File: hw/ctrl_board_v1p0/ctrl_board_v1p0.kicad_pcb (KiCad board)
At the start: 2 copper layers, 65 x 30 mm, 31 parts, among them J1 RaSCSI Connector, J2 OLED Connector, P1 Conn_02x20_Odd_Even, SW1 SW_SPST, SW2 SW_SPST, SW3 SW_SPST, SW4 Rotary_Encoder_Switch, U1 PCA9554APW,118

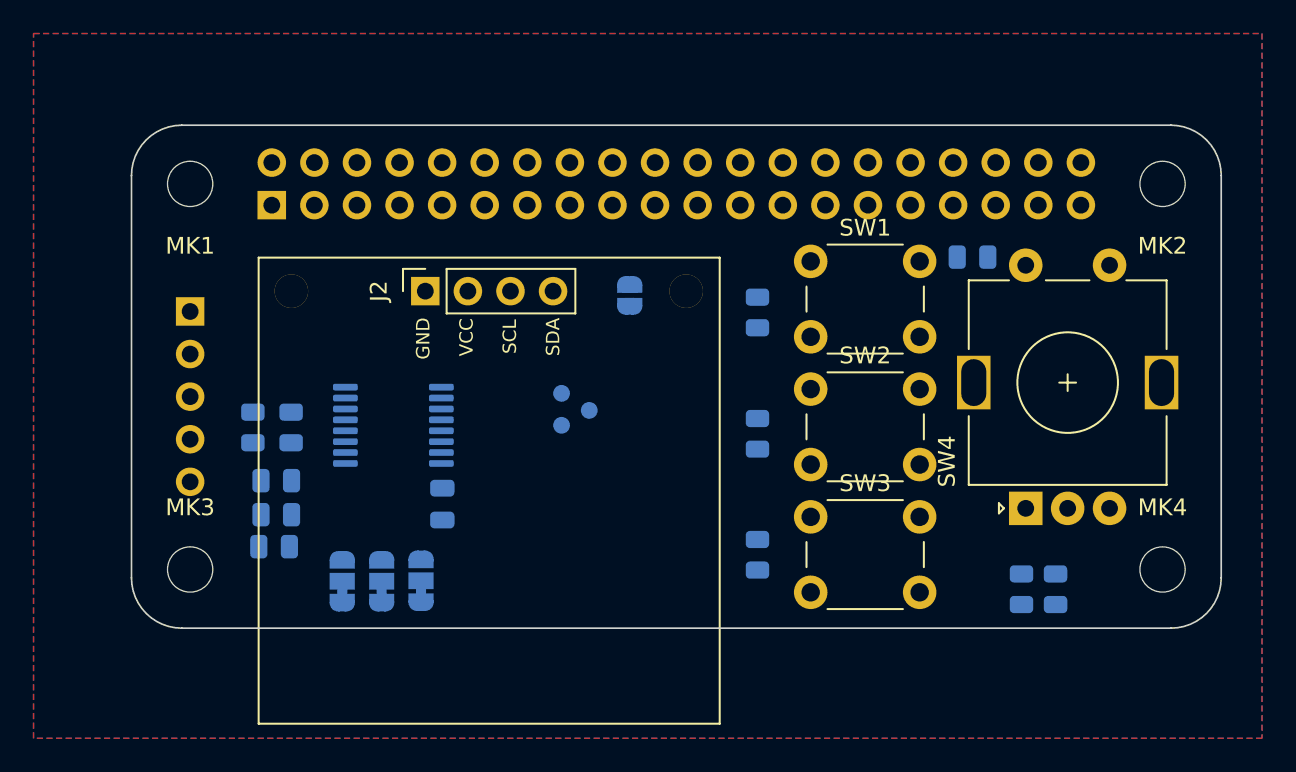
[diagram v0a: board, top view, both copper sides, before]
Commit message: routed signals
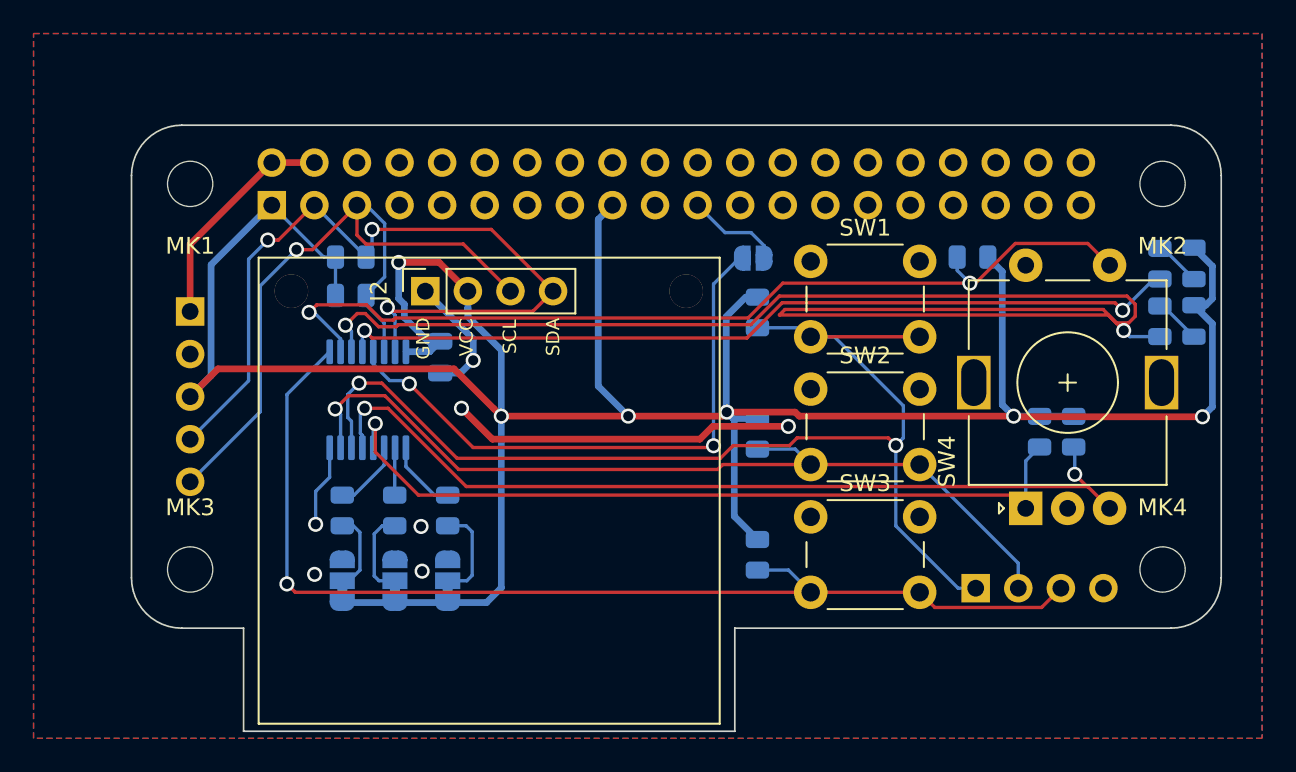
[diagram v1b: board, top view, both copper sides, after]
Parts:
- removed TP1, TP2, TP3: TestPoint_Small, TestPoint:TestPoint_Pad_D1.0mm
- added D1: Green, LED_SMD:LED_0805_2012Metric, B.Cu at (263.4, 105.7)
- added D2: Green, LED_SMD:LED_0805_2012Metric, B.Cu at (263.4, 102.2)
- added J3: Conn_01x04_Male, Connector_PinHeader_2.54mm:PinHeader_1x04_P2.54mm_Vertical, B.Cu at (250.4, 121.6)
- added R12: 10k, Resistor_SMD:R_0805_2012Metric, B.Cu at (261.3, 105.7)
- added R13: 10k, Resistor_SMD:R_0805_2012Metric, B.Cu at (261.3, 102.3)
- moved R11 10.8 mm to (213.1, 101.9), turned to 0 degrees
- moved R7 10.4 mm to (218.9, 117.0), turned to 90 degrees
- moved R10 9.80 mm to (213.1, 104.2), turned to 180 degrees
- moved R1 9.46 mm to (256.2, 112.3), turned to 270 degrees
- moved R2 9.46 mm to (254.2, 112.3), turned to 270 degrees
- moved C1 8.76 mm to (218.4, 107.8)
- moved JP4 7.69 mm to (237.1, 101.9), turned to 0 degrees
- moved R8 7.07 mm to (215.7, 117.0), turned to 90 degrees
- moved R9 4.60 mm to (212.6, 117.0), turned to 90 degrees
- moved U1 2.16 mm to (214.1, 110.4), turned to 90 degrees
- moved JP1 1.59 mm to (218.9, 121.2)
- moved JP2 0.79 mm to (215.7, 121.2)
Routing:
- net +3V3: track 0.00 -> 183.2 mm, vias 0 -> 6
- net Net-(R12-Pad1): track 0.00 -> 96.3 mm, vias 0 -> 2
- net /BUTTON_1: track 0.00 -> 69.6 mm, vias 0 -> 2
- net /BUTTON_3: track 0.00 -> 65.9 mm, vias 0 -> 1
- net /BUTTON_4: track 0.00 -> 55.9 mm, vias 0 -> 2
- net /BUTTON_2: track 0.00 -> 52.9 mm, vias 0 -> 1
- net /ROTARY_ENC_B: track 0.00 -> 52.2 mm, vias 0 -> 2
- net Net-(R13-Pad1): track 0.00 -> 50.8 mm, vias 0 -> 2
- net /GPIO2(SDA1): track 0.00 -> 49.2 mm, vias 0 -> 3
- net /ROTARY_ENC_A: track 0.00 -> 47.7 mm, vias 0 -> 1
- net /GPIO3(SCL1): track 0.00 -> 44.2 mm, vias 0 -> 1
- net Net-(JP4-Pad1): track 0.00 -> 35.1 mm, vias 0 -> 2
- net GND: track 0.00 -> 33.1 mm, vias 0 -> 7
- net +5V: track 0.00 -> 13.4 mm
- net Net-(JP1-Pad2): track 0.00 -> 5.80 mm
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- added copper zone on F.Cu, net GND
- removed copper zone on F.Cu, net (none)
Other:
- board size 65 x 30 mm -> 65 x 36.1 mm

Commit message: Fixed up silkscreens and added mousebites
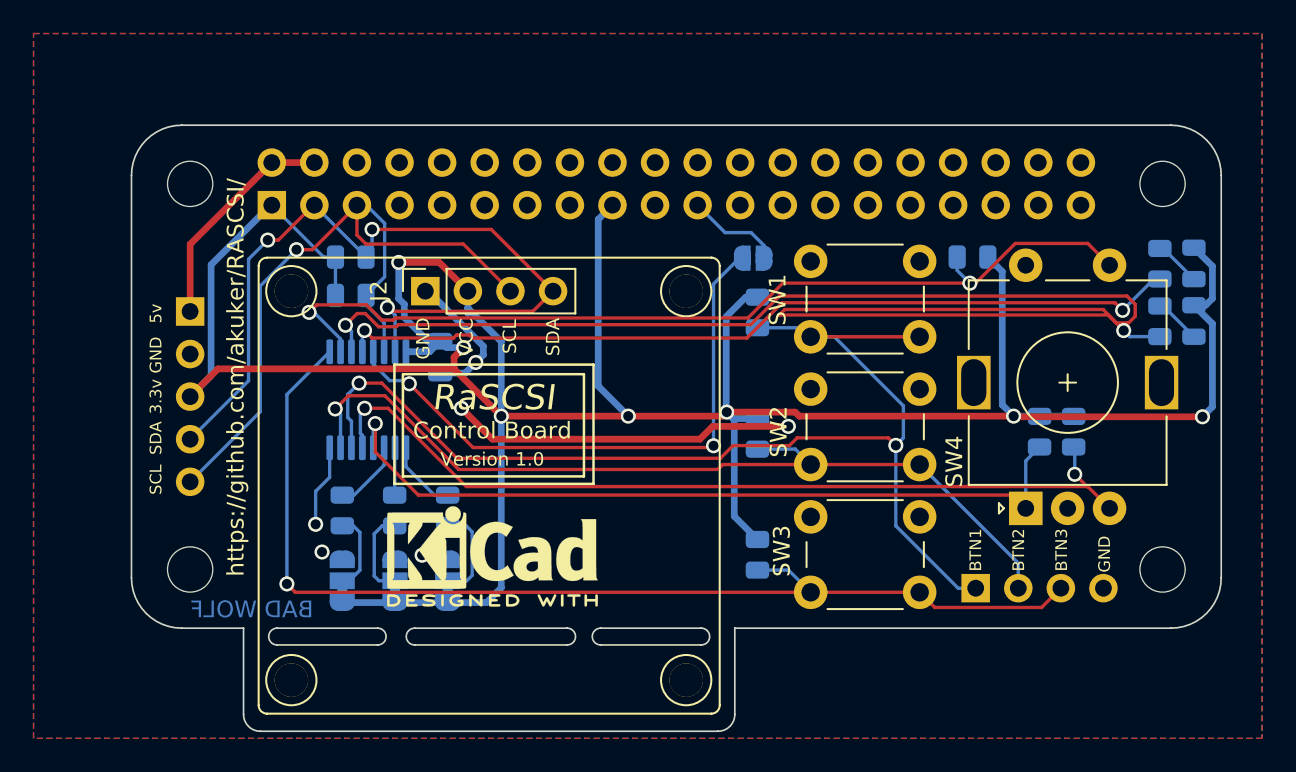
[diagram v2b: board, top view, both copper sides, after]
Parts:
- added G***: LOGO, mousebites:dogcow, B.Cu at (228.9, 109.1)
- added G***: LOGO, mousebites:pi_logo, B.Cu at (208.3, 110.5)
- added REF**: KiCad-Logo2_5mm_SilkScreen, Symbol:KiCad-Logo2_5mm_SilkScreen, F.Cu at (221.5, 119.7)
- J2: footprint Connector_PinSocket_2.54mm:PinSocket_1x04_P2.54mm_Vertical -> mousebites:OLED_Footprint
- JP1, JP2, JP3: footprint Jumper:SolderJumper-3_P1.3mm_Bridged12_RoundedPad1.0x1.5mm -> mousebites:SolderJumper-3_P1.3mm_Bridged12_NoSilkscreen
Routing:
- net +3V3: track 183.2 -> 186.2 mm, vias 6 -> 7
- net GND: track 33.1 -> 33.8 mm, vias 7 -> 6
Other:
- outline, holes or cut-outs redrawn
- board text added: "3.3v"
- board text added: "5v"
- board text added: "A0"
- board text added: "A1"
- board text added: "A2"
- board text added: "BAD WOLF"
- board text added: "BTN1"
- board text added: "BTN2"
- board text added: "BTN3"
- board text added: "Control Board"
- board text added: "GND"
- board text added: "IO Addr"
- board text added: "RaSCSI"
- board text added: "SCL"
- board text added: "SDA"
- board text added: "Vcc"
- board text added: "Version 1.0"
- board text added: "https://github.com/akuker/RASCSI/"

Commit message: cleaned up layout
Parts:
- removed D1, D2: Green, LED_SMD:LED_0805_2012Metric
- removed the G*** at (228.9, 109.1)
- removed REF**: KiCad-Logo2_5mm_SilkScreen, Symbol:KiCad-Logo2_5mm_SilkScreen
- added G***: LOGO, mousebites:dogcow, F.Cu at (227.8, 119.7)
- added G***: LOGO, mousebites:dogcow, F.Cu at (210.5, 119.7)
- J3: value Conn_01x04_Male -> Conn_02x06_Odd_Even; footprint Connector_PinHeader_2.54mm:PinHeader_1x04_P2.54mm_Vertical -> Connector_PinHeader_2.54mm:PinHeader_2x06_P2.54mm_Vertical; moved to F.Cu
- JP1, JP2, JP3: footprint mousebites:SolderJumper-3_P1.3mm_Bridged12_NoSilkscreen -> Jumper:SolderJumper-3_P1.3mm_Bridged12_RoundedPad1.0x1.5mm
- moved G*** 43.0 mm to (251.2, 108.5)
- moved R13 42.5 mm to (223.4, 121.5), turned to 270 degrees
- moved R12 39.3 mm to (225.4, 121.5), turned to 270 degrees
- moved R2 26.6 mm to (228.2, 106.7)
- moved R1 26.6 mm to (230.2, 106.7)
- moved R6 24.5 mm to (226.1, 106.7), turned to 270 degrees
- moved J3 21.7 mm to (260.6, 102.6), turned to 0 degrees
- moved R5 18.5 mm to (224.1, 106.7)
- moved R3 17.4 mm to (220.0, 106.7)
- moved R4 16.3 mm to (222.1, 106.7)
- moved SW4 14.9 mm to (254.0, 102.0), turned to 270 degrees
- moved R11 11.6 mm to (206.4, 111.4), turned to 270 degrees
- moved R10 8.63 mm to (208.4, 111.4), turned to 90 degrees
- moved SW3 4.56 mm to (236.0, 118.0)
- moved SW2 4.52 mm to (236.0, 110.0)
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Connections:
- J3 pad 2: /BUTTON_2 -> GND
- J3 pad 3: /BUTTON_3 -> /BUTTON_2
- R12 pad 1: Net-(R12-Pad1) -> Net-(J3-Pad10)
- R12 pad 2: Net-(D1-Pad1) -> +3V3
- R13 pad 1: Net-(R13-Pad1) -> Net-(J3-Pad12)
- R13 pad 2: Net-(D2-Pad1) -> +3V3
- U1 pad 11: Net-(R12-Pad1) -> /LED_1
- U1 pad 12: Net-(R13-Pad1) -> /LED_2
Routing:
- net +3V3: track 186.2 -> 88.9 mm, vias 7 -> 0
- net Net-(R12-Pad1): track 96.3 -> 0.00 mm, vias 2 -> 0
- net /LED_1: track 0.00 -> 53.9 mm, vias 0 -> 1
- net /LED_2: track 0.00 -> 53.3 mm, vias 0 -> 1
- net Net-(R13-Pad1): track 50.9 -> 0.00 mm, vias 2 -> 0
- net Net-(J3-Pad12): track 0.00 -> 42.9 mm, vias 0 -> 1
- net Net-(J3-Pad10): track 0.00 -> 42.8 mm, vias 0 -> 2
- net /BUTTON_2: track 52.9 -> 71.0 mm, vias 1 -> 3
- net GND: track 33.8 -> 16.0 mm, vias 6 -> 3
- net /BUTTON_1: track 69.6 -> 57.5 mm
- net /BUTTON_3: track 65.9 -> 77.9 mm, vias 1 -> 3
- net Net-(JP4-Pad1): track 35.1 -> 24.8 mm
- net /GPIO2(SDA1): track 49.2 -> 40.9 mm, vias 3 -> 2
- net /BUTTON_4: track 55.9 -> 63.8 mm, vias 2 -> 3
- net /ROTARY_ENC_B: track 52.2 -> 46.0 mm, vias 2 -> 3
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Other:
- board size 65 x 36.1 mm -> 65 x 33 mm
- rule via_min_drill: 0.5 -> 0.2
- rule via_min_size: 0.8 -> 0.4
- board text added: "BTN4"
- board text added: "LED1"
- board text added: "LED2"
- board text added: "RaSCSI Connector"
